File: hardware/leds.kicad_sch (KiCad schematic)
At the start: 16 parts

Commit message: Add the Cube project
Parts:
- removed D? (x3): Red, LED_SMD:LED_0201_0603Metric, symbol Device:LED_Small
- removed R? (x3): 120R, Resistor_SMD:R_0402_1005Metric, symbol Device:R_Small
- added BZ1: Buzzer, symbol Device:Buzzer
- added D?: Red, LED_SMD:LED_0201_0603Metric, symbol Device:LED_Small
- added D?: Green, LED_SMD:LED_0201_0603Metric, symbol Device:LED_Small
- added Q5: PMV450ENEA, symbol Simulation_SPICE:NMOS
- added R?: 100R, Resistor_SMD:R_0603_1608Metric, symbol Device:R_Small
- added R?: 120R, Resistor_SMD:R_0402_1005Metric, symbol Device:R_Small
- added R?: 270R, Resistor_SMD:R_0402_1005Metric, symbol Device:R_Small
- added R?: 10k, Resistor_SMD:R_0603_1608Metric, symbol Device:R_Small
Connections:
- net +3.3V: now also BZ1.1 (-)
- net GND: now also D?.1 (K), D?.1 (K), Q5.3 (S), R?.1
- net FUSE1 renamed FUSE
- new net: Q5.2 (G), R?.1, R?.2
- new net: D?.2 (A), R?.2 (x2)
- new net: BZ1.2 (+), Q5.1 (D)
- new net 5V_AUX: R?.1
- new net BUZZER: R?.2
- new net SAFETY: R?.1
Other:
- title: Ready to Drive Sound -> LEDs
- moved on the sheet: D?, R?

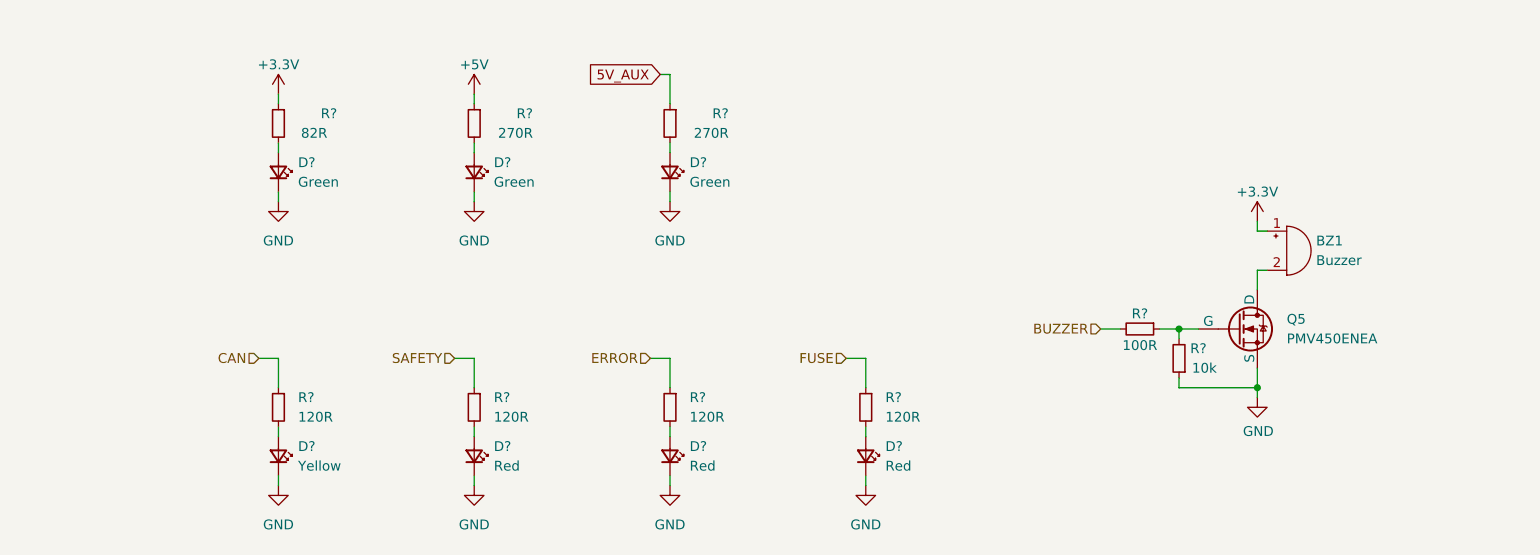
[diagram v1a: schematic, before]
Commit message: Improve the schematic
- add anti-aliasing filters
- rearrange the main connector signals
- improve the power filtering
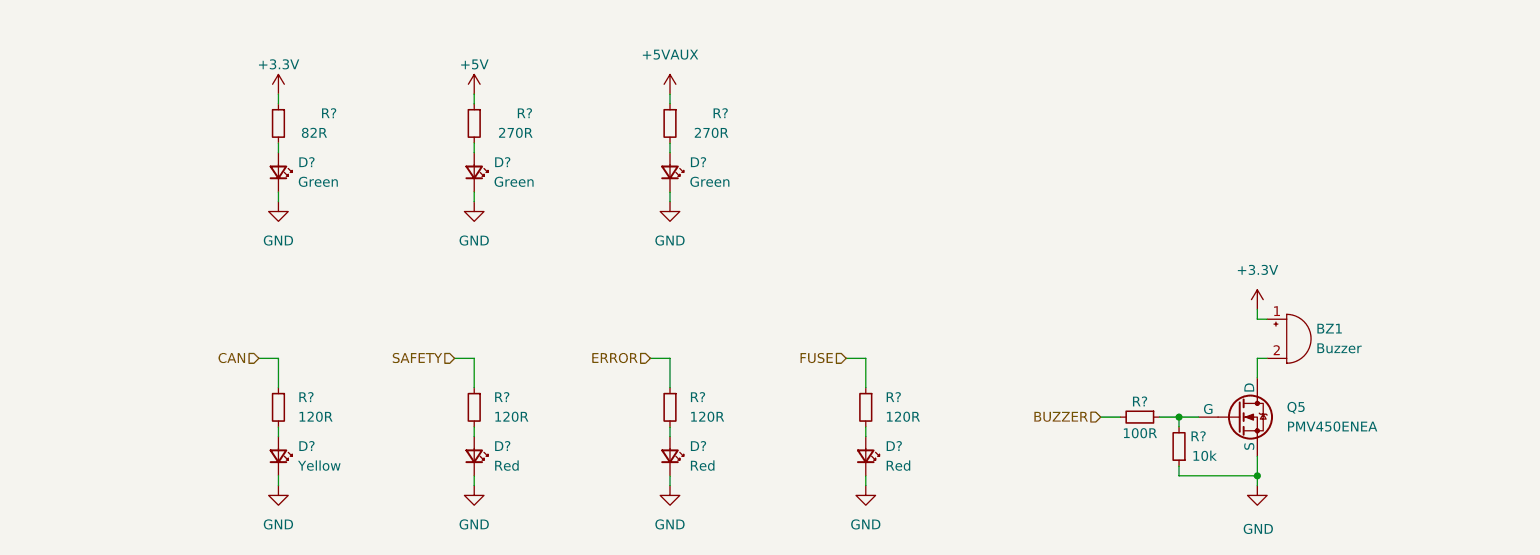
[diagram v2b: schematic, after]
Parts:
- BZ1: footprint (none) -> Buzzer_Beeper:Buzzer_12x9.5RM7.6
- D? (x7): footprint LED_SMD:LED_0201_0603Metric -> LED_SMD:LED_0603_1608Metric
- R? (x7): footprint Resistor_SMD:R_0402_1005Metric -> Resistor_SMD:R_0603_1608Metric
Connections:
- net 5V_AUX renamed +5VAUX
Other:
- moved on the sheet: BZ1, Q5, R?

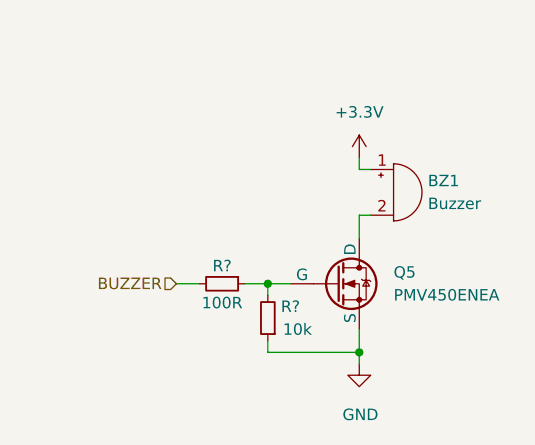
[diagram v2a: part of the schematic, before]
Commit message: Set component values
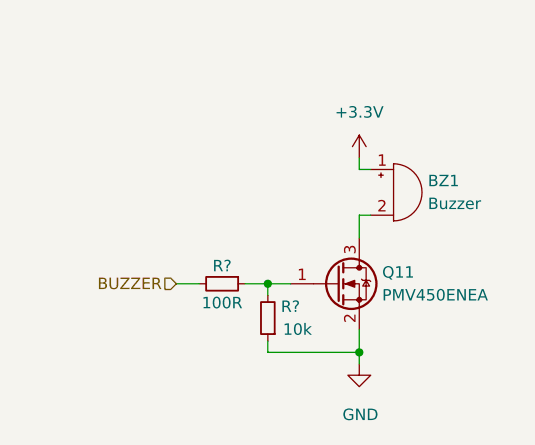
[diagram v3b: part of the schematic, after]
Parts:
- removed Q5: PMV450ENEA, symbol Simulation_SPICE:NMOS
- added Q11: PMV450ENEA, Package_TO_SOT_SMD:SOT-23, symbol Device:Q_NMOS_GSD
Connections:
- net GND: now also Q11.2 (S)
- net at R?.1, R?.2: now also Q11.1 (G)
- net at BZ1.2 (+): now also Q11.3 (D)
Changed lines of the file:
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@@
         )
         (path "/b652b05a-4e3d-4ad1-b032-18886abe7d45/6999686b-4026-4ea7-9227-634603a79198"
-          (reference "R109") (unit 1)
+          (reference "R111") (unit 1)
         )
       )
@@
         )
         (path "/b652b05a-4e3d-4ad1-b032-18886abe7d45/6999686b-4026-4ea7-9227-634603a79198"
-          (reference "R116") (unit 1)
+          (reference "R118") (unit 1)
         )
       )
@@
         )
         (path "/b652b05a-4e3d-4ad1-b032-18886abe7d45/6999686b-4026-4ea7-9227-634603a79198"
-          (reference "R112") (unit 1)
+          (reference "R114") (unit 1)
         )
       )
@@
         )
         (path "/b652b05a-4e3d-4ad1-b032-18886abe7d45/6999686b-4026-4ea7-9227-634603a79198"
-          (reference "R110") (unit 1)
+          (reference "R112") (unit 1)
         )
       )
@@
         )
         (path "/b652b05a-4e3d-4ad1-b032-18886abe7d45/6999686b-4026-4ea7-9227-634603a79198"
-          (reference "R113") (unit 1)
+          (reference "R115") (unit 1)
         )
       )
@@
         )
         (path "/b652b05a-4e3d-4ad1-b032-18886abe7d45/6999686b-4026-4ea7-9227-634603a79198"
-          (reference "R115") (unit 1)
+          (reference "R117") (unit 1)
         )
       )
@@
         )
         (path "/b652b05a-4e3d-4ad1-b032-18886abe7d45/6999686b-4026-4ea7-9227-634603a79198"
-          (reference "R114") (unit 1)
+          (reference "R116") (unit 1)
         )
       )
@@
         )
         (path "/b652b05a-4e3d-4ad1-b032-18886abe7d45/6999686b-4026-4ea7-9227-634603a79198"
-          (reference "R111") (unit 1)
+          (reference "R113") (unit 1)
         )
       )
@@
     )
   )
-  (symbol (lib_id "Simulation_SPICE:NMOS") (at 208.28 118.11 0) (unit 1)
-    (in_bom yes) (on_board yes) (dnp no)
-    (property "Reference" "Q5" (at 214.63 116.84 0)
-      (effects (font (size 1.27 1.27)) (justify left))
-    )
-    (property "Value" "PMV450ENEA" (at 214.63 119.38 0)
-      (effects (font (size 1.27 1.27)) (justify left))
-    )
-    (property "Footprint" "" (at 213.36 115.57 0)
-      (effects (font (size 1.27 1.27)) hide)
-    )
-    (property "Datasheet" "https://assets.nexperia.com/documents/data-sheet/PMV450ENEA.pdf" (at 208.28 130.81 0)
+  (symbol (lib_id "Device:Q_NMOS_GSD") (at 208.28 118.11 0) (unit 1)
+    (in_bom yes) (on_board yes) (dnp no)
+    (property "Reference" "Q11" (at 213.36 116.84 0)
+      (effects (font (size 1.27 1.27)) (justify left))
+    )
+    (property "Value" "PMV450ENEA" (at 213.36 119.38 0)
+      (effects (font (size 1.27 1.27)) (justify left))
+    )
+    (property "Footprint" "Package_TO_SOT_SMD:SOT-23" (at 213.36 115.57 0)
+      (effects (font (size 1.27 1.27)) hide)
+    )
+    (property "Datasheet" "https://assets.nexperia.com/documents/data-sheet/PMV450ENEA.pdf" (at 208.28 118.11 0)
       (effects (font (size 1.27 1.27)) hide)
     )
@@
     (instances
       (project "rearbox"
-        (path "/b652b05a-4e3d-4ad1-b032-18886abe7d45/91248db3-ac16-4fb7-9cfe-25145bb94249"
-          (reference "Q5") (unit 1)
-        )
-        (path "/b652b05a-4e3d-4ad1-b032-18886abe7d45/562e38ba-d94a-4627-8fa0-e9eb7b5e4e9a"
-          (reference "Q11") (unit 1)
-        )
         (path "/b652b05a-4e3d-4ad1-b032-18886abe7d45/6999686b-4026-4ea7-9227-634603a79198"
           (reference "Q11") (unit 1)
@@
         )
         (path "/b652b05a-4e3d-4ad1-b032-18886abe7d45/6999686b-4026-4ea7-9227-634603a79198"
-          (reference "R117") (unit 1)
-        )
-      )
+          (reference "R119") (unit 1)
+        )
+      )

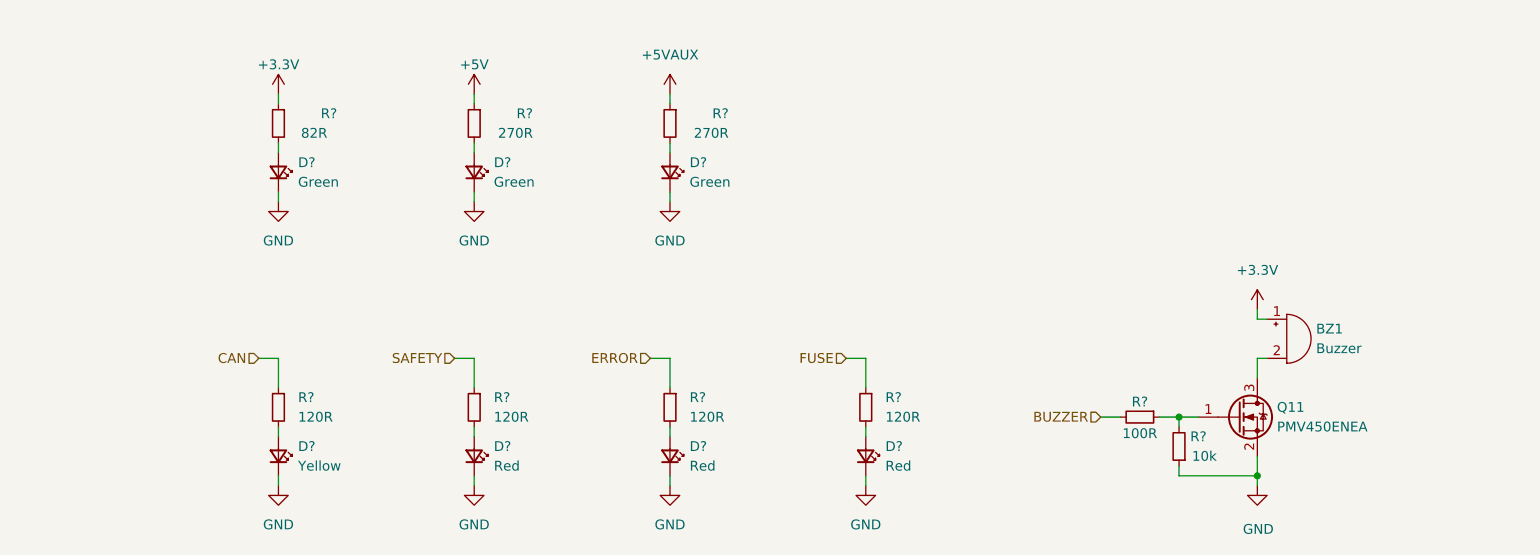
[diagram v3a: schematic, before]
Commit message: Improve the schematic according to the feedback
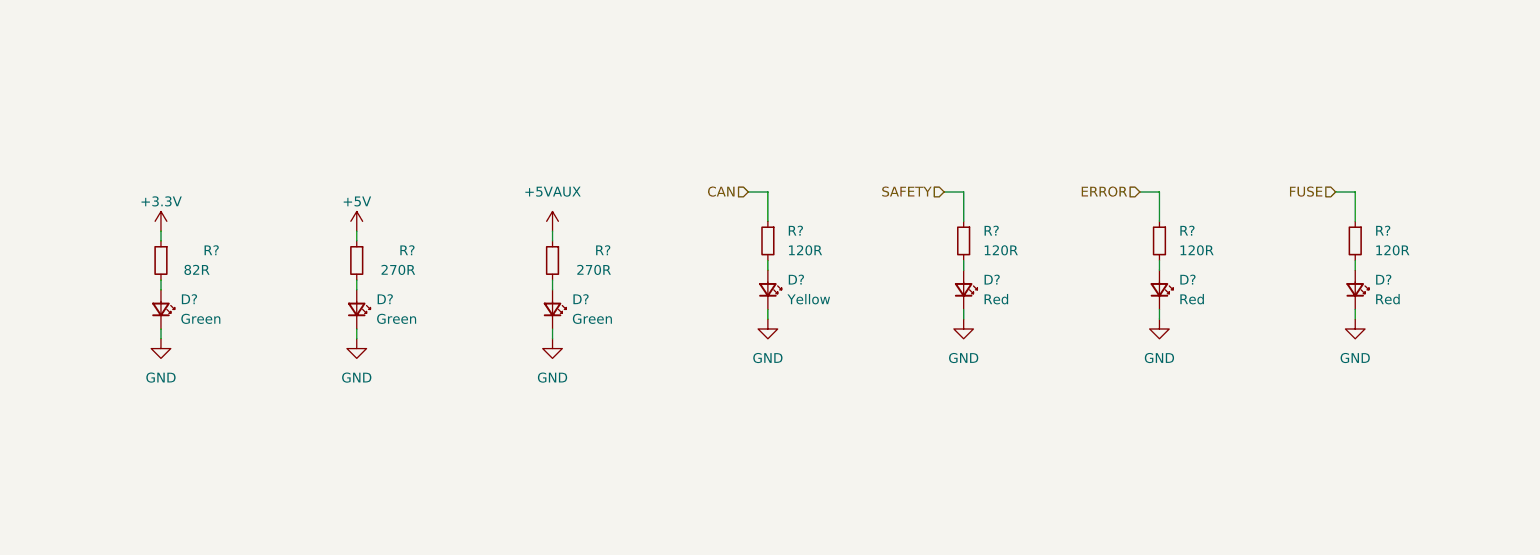
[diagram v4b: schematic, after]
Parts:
- removed BZ1: Buzzer, Buzzer_Beeper:Buzzer_12x9.5RM7.6, symbol Device:Buzzer
- removed D?: Yellow, LED_SMD:LED_0603_1608Metric, symbol Device:LED_Small
- removed D? (x3): Red, LED_SMD:LED_0603_1608Metric, symbol Device:LED_Small
- removed D? (x3): Green, LED_SMD:LED_0603_1608Metric, symbol Device:LED_Small
- removed Q11: PMV450ENEA, Package_TO_SOT_SMD:SOT-23, symbol Device:Q_NMOS_GSD
- removed R?: 82R, Resistor_SMD:R_0603_1608Metric, symbol Device:R_Small
- removed R?: 100R, Resistor_SMD:R_0603_1608Metric, symbol Device:R_Small
- removed R? (x4): 120R, Resistor_SMD:R_0603_1608Metric, symbol Device:R_Small
- removed R? (x2): 270R, Resistor_SMD:R_0603_1608Metric, symbol Device:R_Small
- removed R?: 10k, Resistor_SMD:R_0603_1608Metric, symbol Device:R_Small
- added D? (x3): Green, LED_SMD:LED_0603_1608Metric, symbol Device:LED_Small
- added D?: Yellow, LED_SMD:LED_0603_1608Metric, symbol Device:LED_Small
- added D? (x3): Red, LED_SMD:LED_0603_1608Metric, symbol Device:LED_Small
- added R? (x4): 120R, Resistor_SMD:R_0603_1608Metric, symbol Device:R_Small
- added R? (x2): 270R, Resistor_SMD:R_0603_1608Metric, symbol Device:R_Small
- added R?: 82R, Resistor_SMD:R_0603_1608Metric, symbol Device:R_Small
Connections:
- net +3.3V: now also R?.1
- net +5V: now also R?.1
- net +5VAUX: now also R?.1
- net CAN: now also R?.1
- net ERROR: now also R?.1
- net FUSE: now also R?.1
- net GND: now also D?.1 (K), D?.1 (K), D?.1 (K), D?.1 (K), D?.1 (K), D?.1 (K), D?.1 (K)
- net SAFETY: now also R?.1
- new net: D?.2 (A), R?.2 (x7)

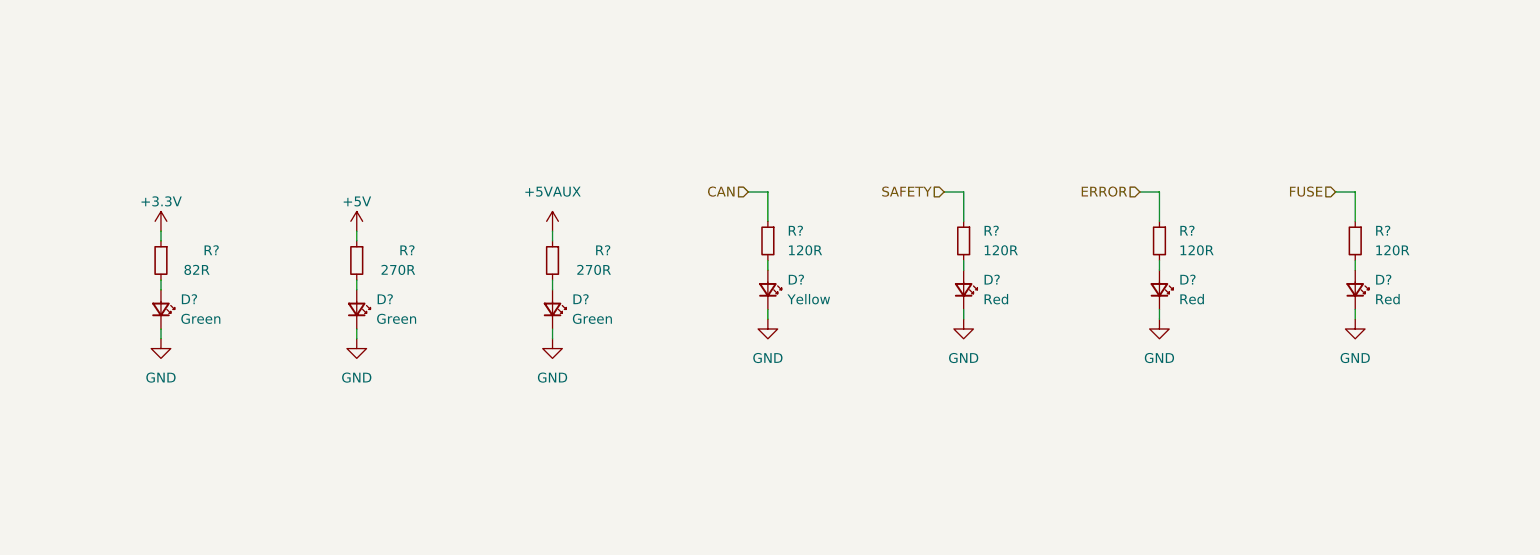
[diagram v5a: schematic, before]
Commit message: Improve the diagram based on the feedback
- add an input LC filter
- remove the USB connector
- add a programmer connector
- move optocouplers into a subsheet
- add a suspension tension meter IC
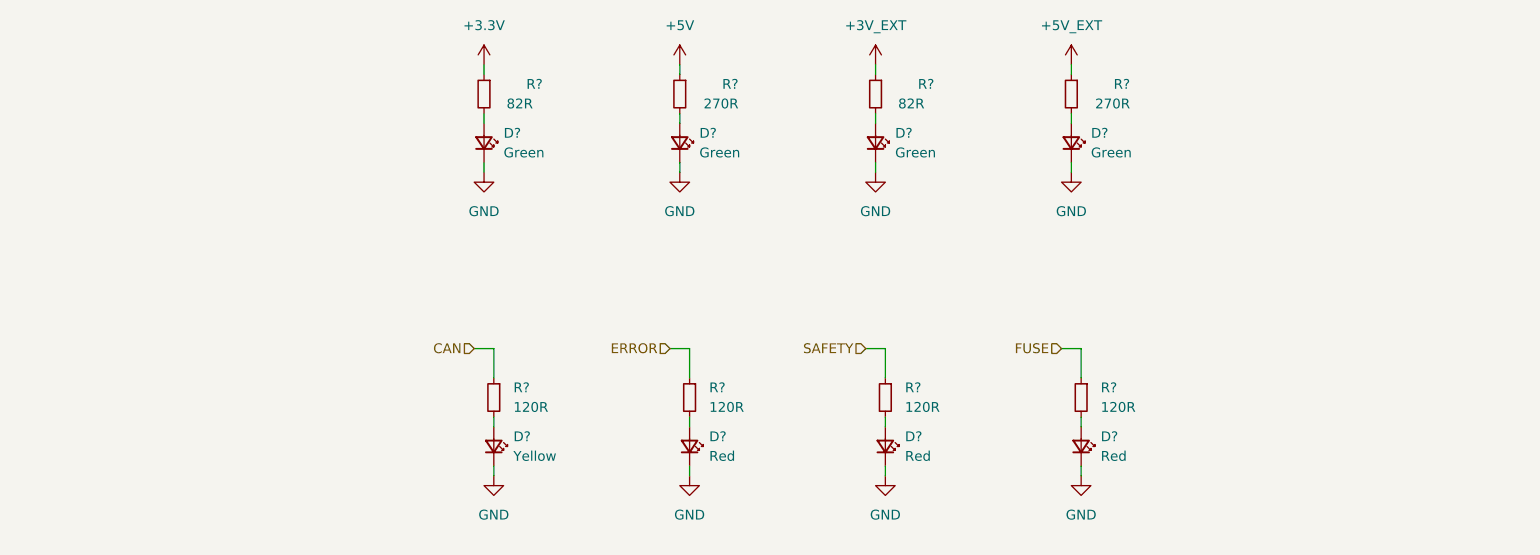
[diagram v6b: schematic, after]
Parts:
- added D?: Green, LED_SMD:LED_0603_1608Metric, symbol Device:LED_Small
- added R?: 82R, Resistor_SMD:R_0603_1608Metric, symbol Device:R_Small
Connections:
- net ERROR: now also R?.1; no longer R?.1
- net GND: now also D?.1 (K)
- net SAFETY: now also R?.1; no longer R?.1
- net +5VAUX renamed +5V_EXT
- new net: D?.2 (A), R?.2
- new net +3V_EXT: R?.1
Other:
- moved on the sheet: D?, R?
